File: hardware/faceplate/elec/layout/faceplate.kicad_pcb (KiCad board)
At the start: 2 copper layers, 181.9 x 127.5 mm, 70 parts

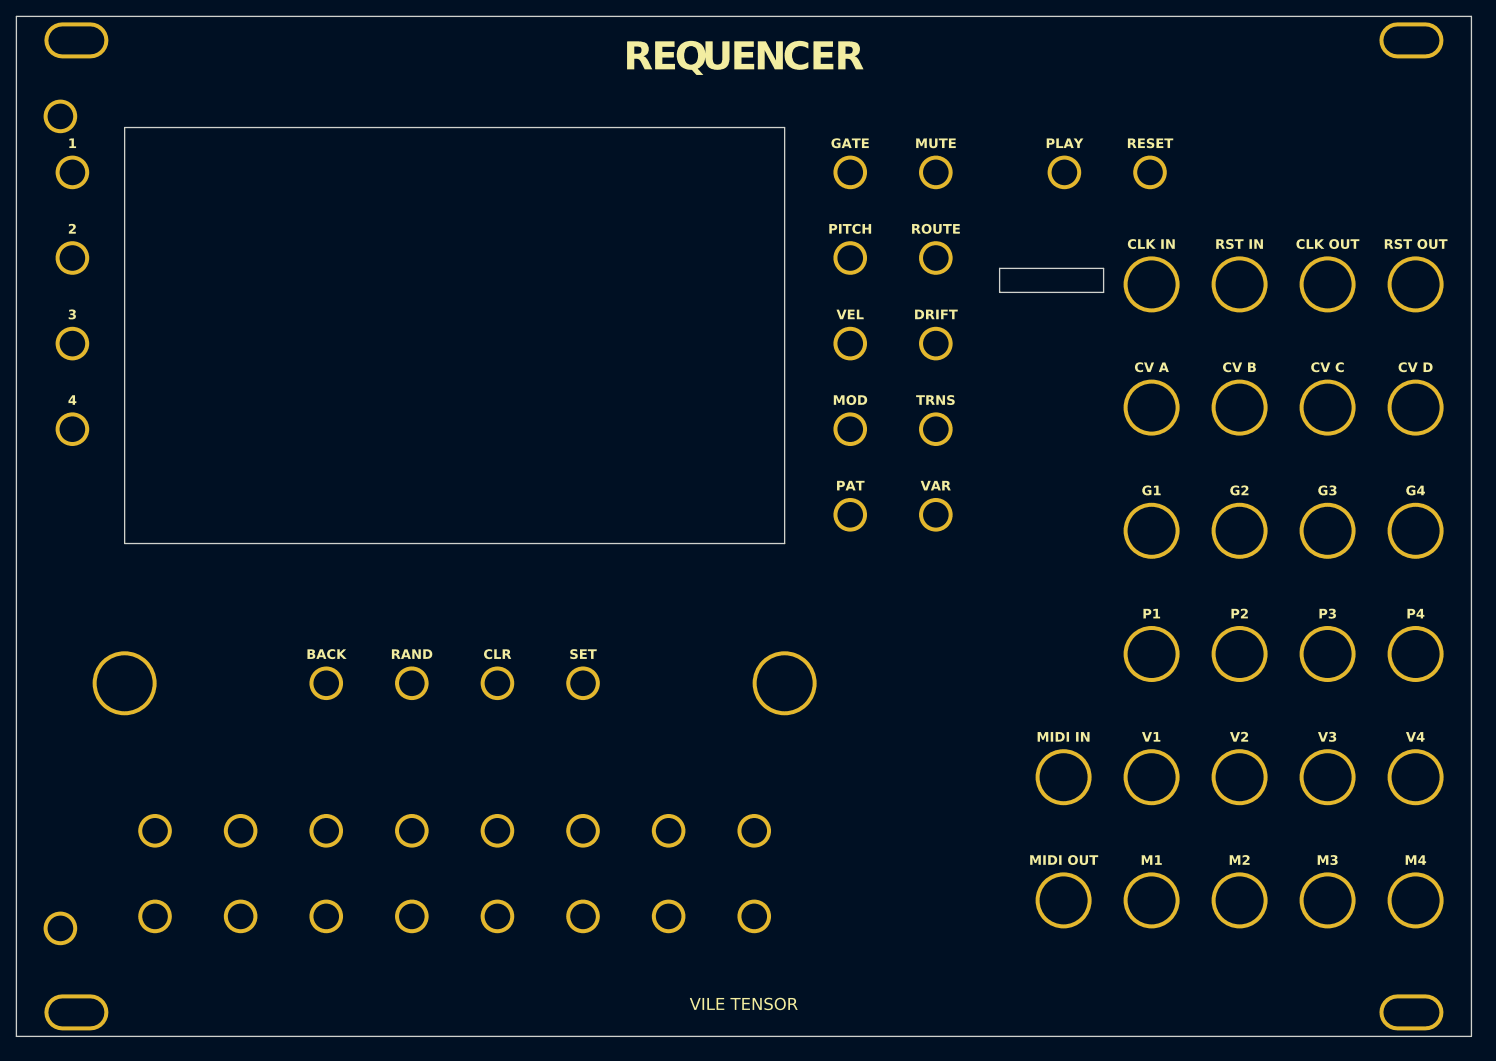
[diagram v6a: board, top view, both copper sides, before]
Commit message: Update parts and placement algos
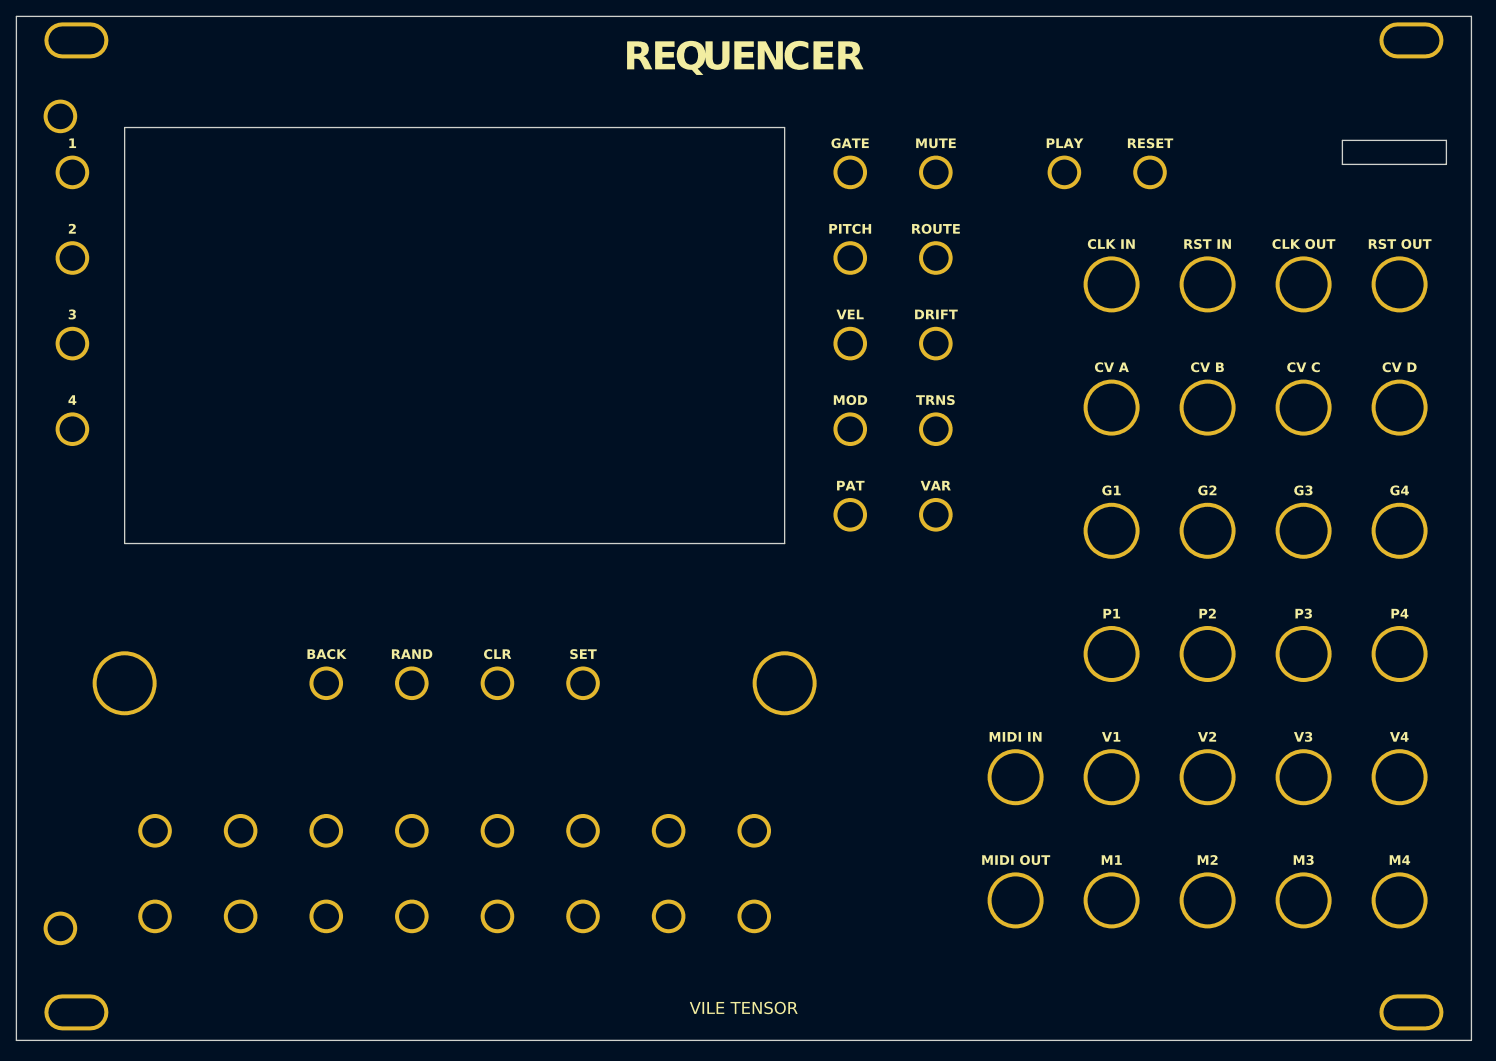
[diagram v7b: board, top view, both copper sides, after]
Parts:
- moved J7 6.00 mm to (124.9, 95.1)
- moved J8 6.00 mm to (124.9, 110.5)
- moved J13 5.00 mm to (136.9, 64.3)
- moved J17 5.00 mm to (136.9, 79.7)
- moved J21 5.00 mm to (136.9, 95.1)
- moved J25 5.00 mm to (136.9, 110.5)
- moved J29 5.00 mm to (136.9, 48.9)
- moved J9 5.00 mm to (136.9, 33.5)
- moved J11 4.00 mm to (148.9, 33.5)
- moved J14 4.00 mm to (148.9, 64.3)
- moved J18 4.00 mm to (148.9, 79.7)
- moved J22 4.00 mm to (148.9, 95.1)
- moved J26 4.00 mm to (148.9, 110.5)
- moved J30 4.00 mm to (148.9, 48.9)
- moved J10 3.00 mm to (160.9, 33.5)
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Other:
- board size 181.9 x 127.5 mm -> 181.9 x 128 mm

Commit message: Routing hell.. broken
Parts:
- moved SW46 0.75 mm to (17.3, 101.0)
- moved SW47 0.75 mm to (28.0, 101.0)
- moved SW48 0.75 mm to (38.7, 101.0)
- moved SW49 0.75 mm to (49.4, 101.0)
- moved SW50 0.75 mm to (60.1, 101.0)
- moved SW51 0.75 mm to (70.8, 101.0)
- moved SW52 0.75 mm to (81.5, 101.0)
- moved SW53 0.75 mm to (92.2, 101.0)
- moved SW54 0.75 mm to (17.3, 111.8)
- moved SW55 0.75 mm to (28.0, 111.8)
- moved SW56 0.75 mm to (38.7, 111.8)
- moved SW57 0.75 mm to (49.4, 111.8)
- moved SW58 0.75 mm to (60.1, 111.8)
- moved SW59 0.75 mm to (70.8, 111.8)
- moved SW60 0.75 mm to (81.5, 111.8)
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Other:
- outline, holes or cut-outs redrawn
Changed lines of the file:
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@@
     (pad "1" thru_hole circle (at 0 0) (size 4.200 4.200) (drill 3.200) (layers "*.Cu" "*.Mask"))
   )
-  (gr_line (start 13.530 13.890) (end 96.030 13.890) (layer "Edge.Cuts") (width 0.1))
-  (gr_line (start 96.030 13.890) (end 96.030 65.890) (layer "Edge.Cuts") (width 0.1))
-  (gr_line (start 96.030 65.890) (end 13.530 65.890) (layer "Edge.Cuts") (width 0.1))
-  (gr_line (start 13.530 65.890) (end 13.530 13.890) (layer "Edge.Cuts") (width 0.1))
+  (gr_line (start 14.030 13.740) (end 95.530 13.740) (layer "Edge.Cuts") (width 0.1))
+  (gr_line (start 95.530 13.740) (end 95.530 66.040) (layer "Edge.Cuts") (width 0.1))
+  (gr_line (start 95.530 66.040) (end 14.030 66.040) (layer "Edge.Cuts") (width 0.1))
+  (gr_line (start 14.030 66.040) (end 14.030 13.740) (layer "Edge.Cuts") (width 0.1))
   (footprint "Faceplate:J7" (layer "F.Cu")
     (at 124.900 95.100)
@@
     (fp_text user "VAR" (at 0 -3.600) (layer "F.SilkS") (effects (font (face "JetBrains Mono") (size 1.2 1.2) (thickness 0.35) (bold yes))))  )
   (footprint "Faceplate:SW46" (layer "F.Cu")
-    (at 17.330 101.800)
+    (at 17.330 101.050)
     (attr exclude_from_pos_files exclude_from_bom)
     (fp_text reference "SW46" (at 0 -3.100) (layer "F.Fab") (effects (font (size 1 1) (thickness 0.15))))
@@
   )
   (footprint "Faceplate:SW47" (layer "F.Cu")
-    (at 28.030 101.800)
+    (at 28.030 101.050)
     (attr exclude_from_pos_files exclude_from_bom)
     (fp_text reference "SW47" (at 0 -3.100) (layer "F.Fab") (effects (font (size 1 1) (thickness 0.15))))
@@
   )
   (footprint "Faceplate:SW48" (layer "F.Cu")
-    (at 38.730 101.800)
+    (at 38.730 101.050)
     (attr exclude_from_pos_files exclude_from_bom)
     (fp_text reference "SW48" (at 0 -3.100) (layer "F.Fab") (effects (font (size 1 1) (thickness 0.15))))
@@
   )
   (footprint "Faceplate:SW49" (layer "F.Cu")
-    (at 49.430 101.800)
+    (at 49.430 101.050)
     (attr exclude_from_pos_files exclude_from_bom)
     (fp_text reference "SW49" (at 0 -3.100) (layer "F.Fab") (effects (font (size 1 1) (thickness 0.15))))
@@
   )
   (footprint "Faceplate:SW50" (layer "F.Cu")
-    (at 60.130 101.800)
+    (at 60.130 101.050)
     (attr exclude_from_pos_files exclude_from_bom)
     (fp_text reference "SW50" (at 0 -3.100) (layer "F.Fab") (effects (font (size 1 1) (thickness 0.15))))
@@
   )
   (footprint "Faceplate:SW51" (layer "F.Cu")
-    (at 70.830 101.800)
+    (at 70.830 101.050)
     (attr exclude_from_pos_files exclude_from_bom)
     (fp_text reference "SW51" (at 0 -3.100) (layer "F.Fab") (effects (font (size 1 1) (thickness 0.15))))
@@
   )
   (footprint "Faceplate:SW52" (layer "F.Cu")
-    (at 81.530 101.800)
+    (at 81.530 101.050)
     (attr exclude_from_pos_files exclude_from_bom)
     (fp_text reference "SW52" (at 0 -3.100) (layer "F.Fab") (effects (font (size 1 1) (thickness 0.15))))
@@
   )
   (footprint "Faceplate:SW53" (layer "F.Cu")
-    (at 92.230 101.800)
+    (at 92.230 101.050)
     (attr exclude_from_pos_files exclude_from_bom)
     (fp_text reference "SW53" (at 0 -3.100) (layer "F.Fab") (effects (font (size 1 1) (thickness 0.15))))
@@
   )
   (footprint "Faceplate:SW54" (layer "F.Cu")
-    (at 17.330 112.500)
+    (at 17.330 111.750)
     (attr exclude_from_pos_files exclude_from_bom)
     (fp_text reference "SW54" (at 0 -3.100) (layer "F.Fab") (effects (font (size 1 1) (thickness 0.15))))
@@
   )
   (footprint "Faceplate:SW55" (layer "F.Cu")
-    (at 28.030 112.500)
+    (at 28.030 111.750)
     (attr exclude_from_pos_files exclude_from_bom)
     (fp_text reference "SW55" (at 0 -3.100) (layer "F.Fab") (effects (font (size 1 1) (thickness 0.15))))
@@
   )
   (footprint "Faceplate:SW56" (layer "F.Cu")
-    (at 38.730 112.500)
+    (at 38.730 111.750)
     (attr exclude_from_pos_files exclude_from_bom)
     (fp_text reference "SW56" (at 0 -3.100) (layer "F.Fab") (effects (font (size 1 1) (thickness 0.15))))
@@
   )
   (footprint "Faceplate:SW57" (layer "F.Cu")
-    (at 49.430 112.500)
+    (at 49.430 111.750)
     (attr exclude_from_pos_files exclude_from_bom)
     (fp_text reference "SW57" (at 0 -3.100) (layer "F.Fab") (effects (font (size 1 1) (thickness 0.15))))
@@
   )
   (footprint "Faceplate:SW58" (layer "F.Cu")
-    (at 60.130 112.500)
+    (at 60.130 111.750)
     (attr exclude_from_pos_files exclude_from_bom)
     (fp_text reference "SW58" (at 0 -3.100) (layer "F.Fab") (effects (font (size 1 1) (thickness 0.15))))
@@
   )
   (footprint "Faceplate:SW59" (layer "F.Cu")
-    (at 70.830 112.500)
+    (at 70.830 111.750)
     (attr exclude_from_pos_files exclude_from_bom)
     (fp_text reference "SW59" (at 0 -3.100) (layer "F.Fab") (effects (font (size 1 1) (thickness 0.15))))
@@
   )
   (footprint "Faceplate:SW60" (layer "F.Cu")
-    (at 81.530 112.500)
+    (at 81.530 111.750)
     (attr exclude_from_pos_files exclude_from_bom)
     (fp_text reference "SW60" (at 0 -3.100) (layer "F.Fab") (effects (font (size 1 1) (thickness 0.15))))
@@
   )
   (footprint "Faceplate:SW61" (layer "F.Cu")
-    (at 92.230 112.500)
+    (at 92.230 111.750)
     (attr exclude_from_pos_files exclude_from_bom)
     (fp_text reference "SW61" (at 0 -3.100) (layer "F.Fab") (effects (font (size 1 1) (thickness 0.15))))
